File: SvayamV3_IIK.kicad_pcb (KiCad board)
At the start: 6 copper layers, 50 x 70 mm, 164 parts, among them J1 USB_C_Receptacle_USB2.0_16P, J10 POWER2, J11 TELEM1, J12 TELEM2, J13 GPS, J14 SERIAL4, J15 SERIAL5, J16 I2C, J17 CAN, J18 BUZZER, J19 SWD, J2 Micro_SD_Card_Det1, J20 ADC, J21 SPI, J22 SAFETY, J23 CAN2, J24 SBUS, J3 S_TOP_SIG, J4 S_TOP_PWR, J5 S_TOP_GND, J6 S_SIDE_SIG, J7 S_SIDE_PWR, J8 S_SIDE_GND, J9 POWER1, Q1 AO3400A, SW1 TS-1010A-B, SW2 SK-3296S-01-L3, U1 STM32H743IIKx, U10 RT9080-33GJ5, U11 AP22804AW5, U12 USBLC6-2SC6, U13 TJA1051TK-3, U2 TJA1051TK-3, U3 FM25CL64B, U4 BMI088, U5 BMI270, U6 BMP388, U7 BMM150, U8 TPS2120YFPR, U9 RT9080-33GJ5, Y1 X50328MSB2GI

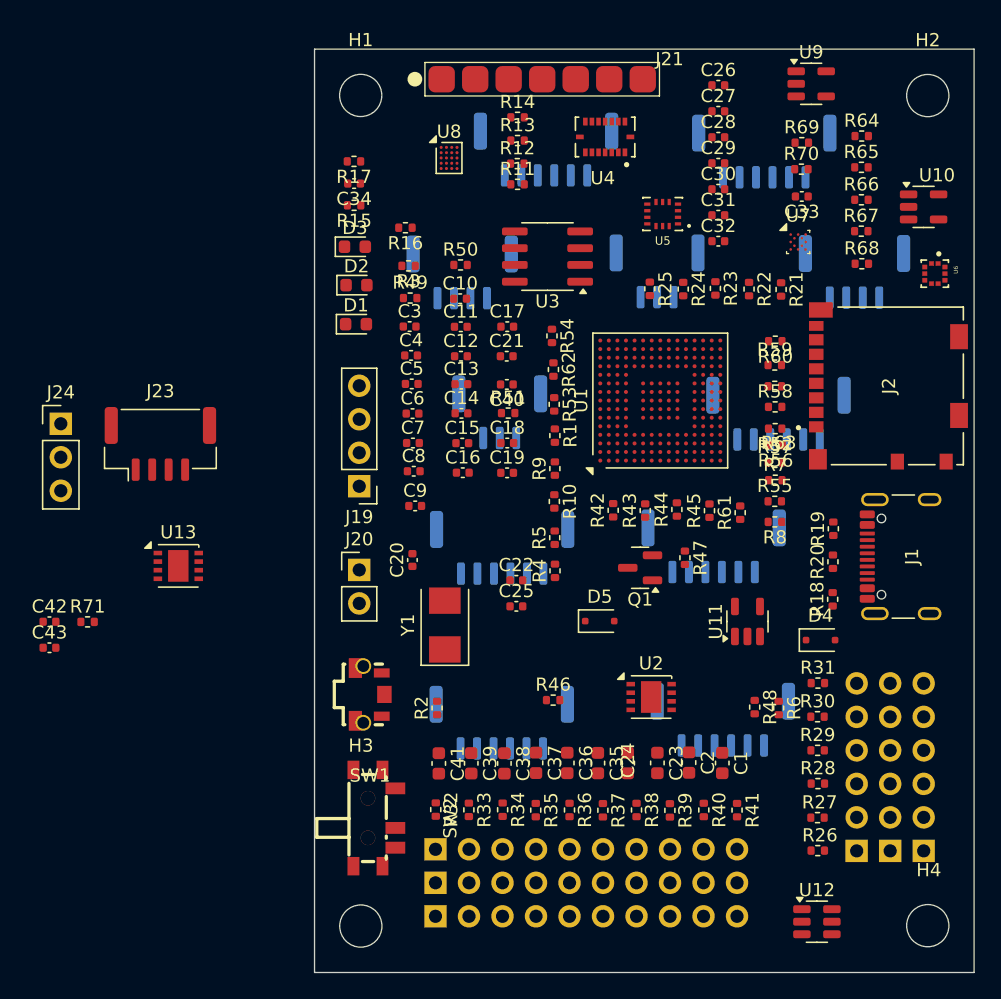
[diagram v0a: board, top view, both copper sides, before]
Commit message: Schematic Changes on MPN and Footprint
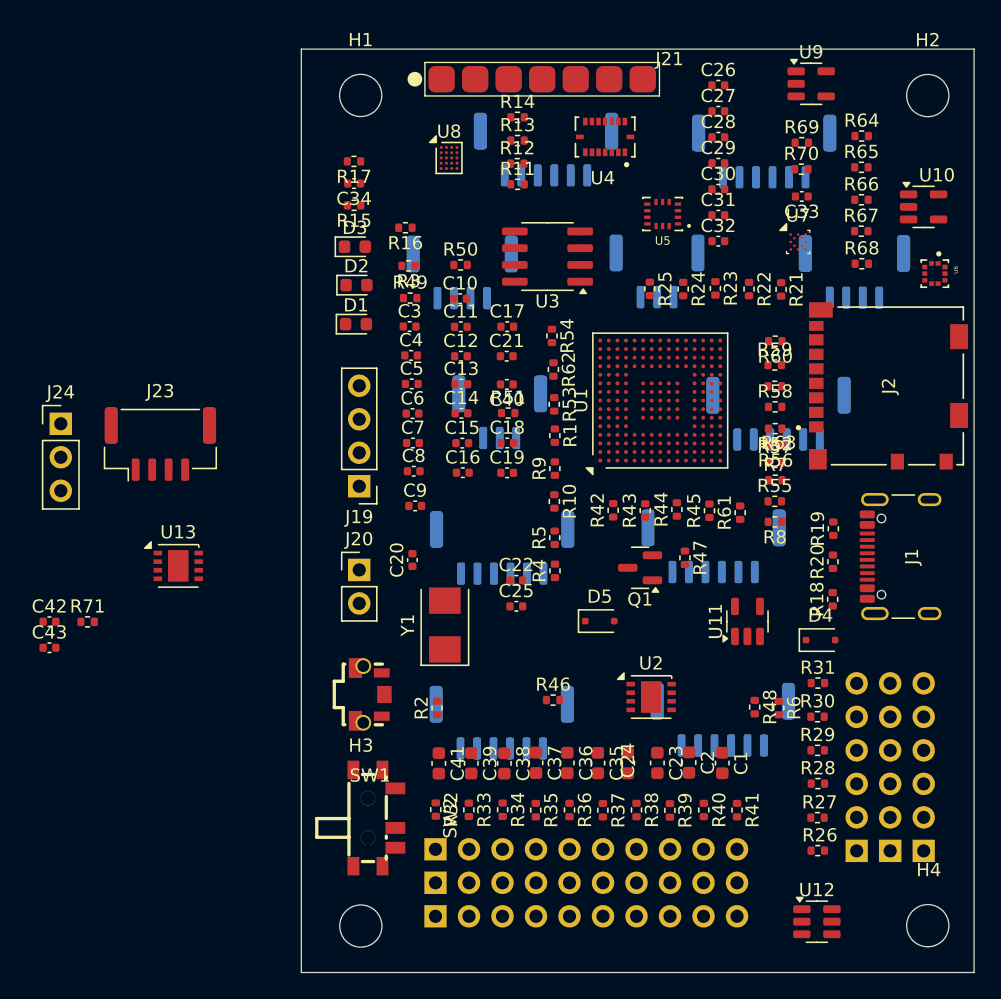
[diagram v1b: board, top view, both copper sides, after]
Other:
- board size 50 x 70 mm -> 51 x 70 mm
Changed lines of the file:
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@@
 	)
 	(gr_rect
-		(start 103.84 34.79)
+		(start 102.84 34.79)
 		(end 153.84 104.79)
 		(stroke
